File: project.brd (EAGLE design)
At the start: 160 x 100 mm, 42 parts, among them Y1 ABM8-20.000MHZ-B2-T

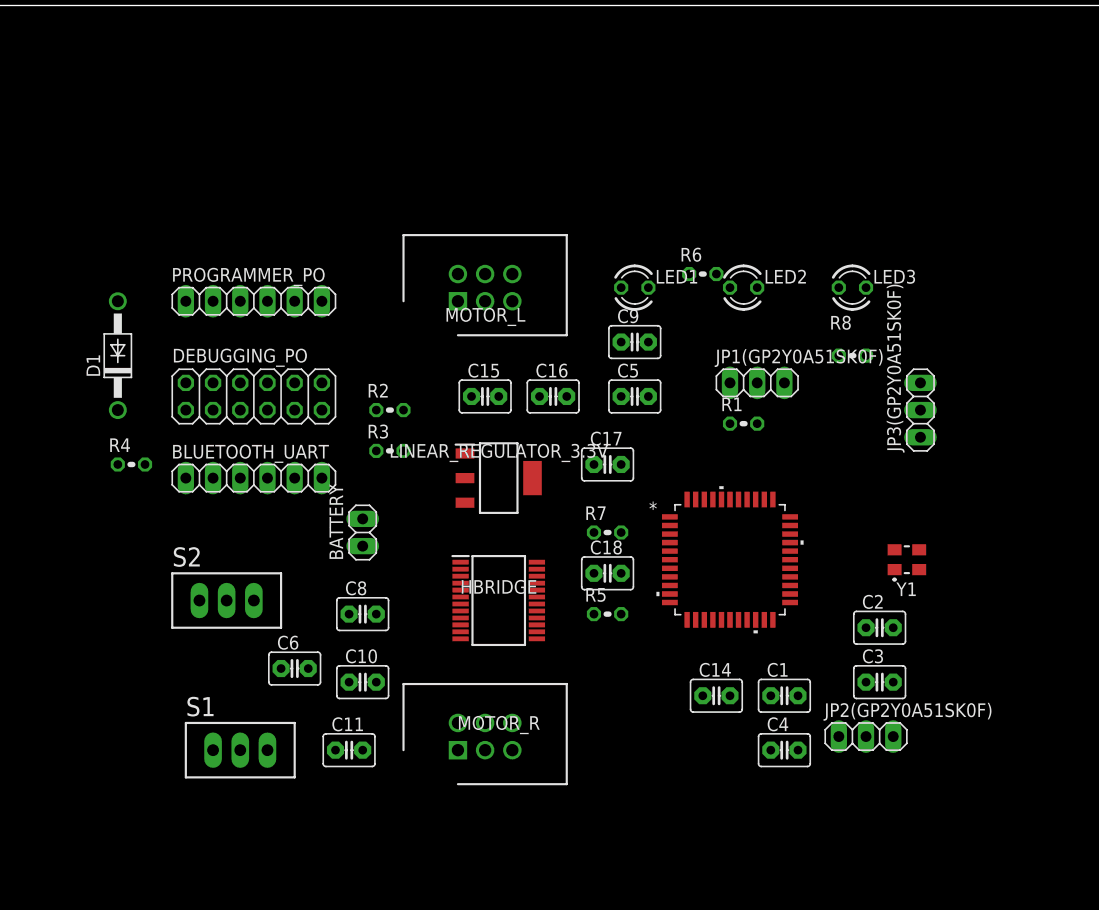
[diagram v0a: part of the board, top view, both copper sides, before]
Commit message: group and place components in board
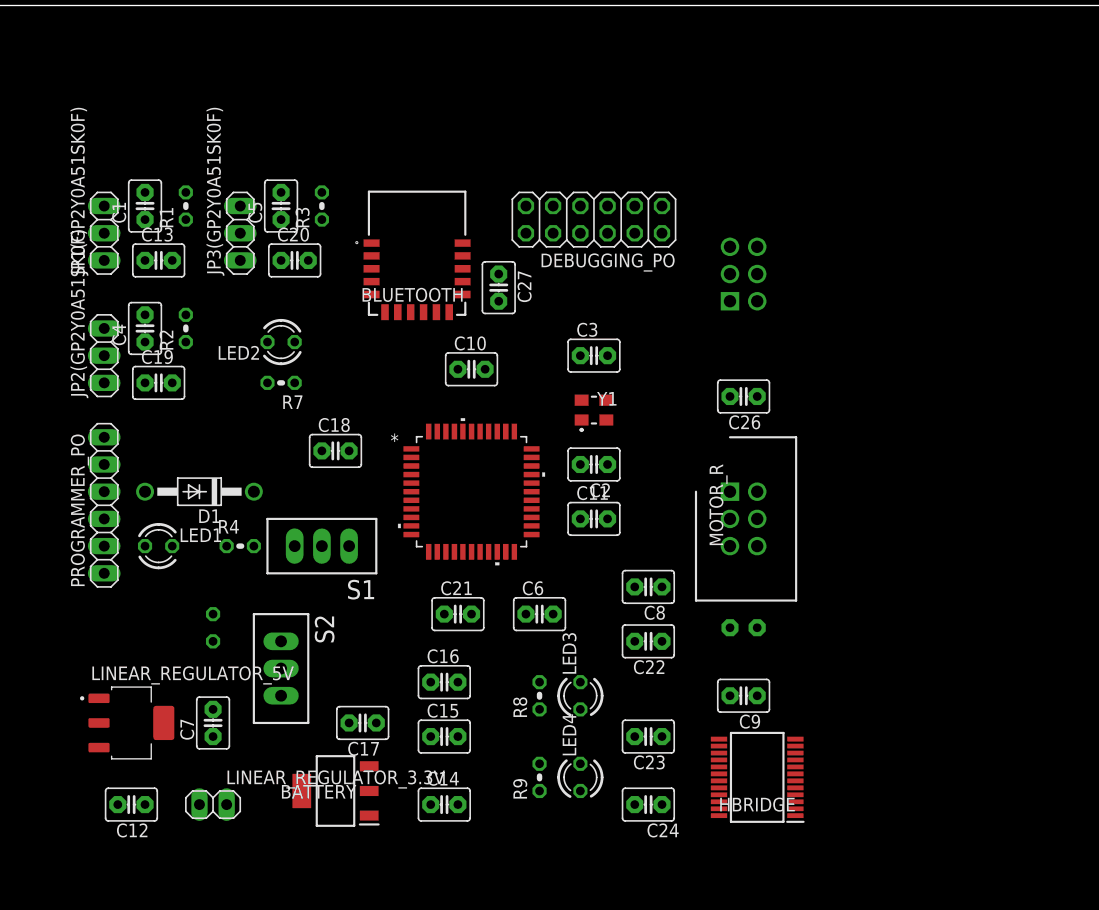
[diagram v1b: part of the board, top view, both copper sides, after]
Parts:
- removed BLUETOOTH_UART: (no value), pinhead:1X06
- removed R6: 10k, rcl:0204V
- added BLUETOOTH: RN4871-I_RM130, RN4871-I_RM130:RN4871
- added C12, C7: 1uF, capacitor-wima:C2.5-3
- added C13, C19, C20, C21, C24, C25, C26, C27: 100nF, capacitor-wima:C2.5-3
- added C22: 0.1uF, capacitor-wima:C2.5-3
- added C23: 10uF, capacitor-wima:C2.5-3
- added LED4: TLLG4400, led:LED3MM
- added LINEAR_REGULATOR_5V: ADP3338AKCZ-5-R7, ADP3338AKCZ-5-R7:SOT230P700X180-4N
- added R9: 10k, rcl:0204V
- C10, C11, C6: value 0.1uF -> 100nF
- C8: value 0.1uF -> 10uF
- moved JP2(GP2Y0A51SK0F) 79.5 mm to (41.9, 67.3), turned to 90 degrees
- moved C1 75.2 mm to (45.7, 81.3), turned to 90 degrees
- moved C4 71.5 mm to (45.7, 69.8), turned to 90 degrees
- moved JP3(GP2Y0A51SK0F) 65.6 mm to (54.6, 78.7)
- moved JP1(GP2Y0A51SK0F) 62.5 mm to (41.9, 78.7), turned to 90 degrees
- moved R1 55.9 mm to (49.5, 81.3), turned to 90 degrees
- moved LED1 50.6 mm to (47.0, 49.5)
- moved LED3 45.8 mm to (86.4, 35.6), turned to 90 degrees
- moved LED2 43.5 mm to (58.4, 68.6), turned to 180 degrees
- moved R8 43.1 mm to (82.5, 35.6), turned to 90 degrees
- moved C3 40.5 mm to (87.6, 67.3)
- moved C5 37.5 mm to (58.4, 81.3), turned to 90 degrees
- moved R5 36.9 mm to (52.1, 41.9), flipped to the bottom, turned to 270 degrees
- moved DEBUGGING_PO 35.8 mm to (87.6, 80.0), turned to 180 degrees
- moved MOTOR_R 35.0 mm to (100.3, 54.6), turned to 270 degrees
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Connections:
- removed net CTS: BLUETOOTH_UART.6, MICROCHIP.10
- removed net ENCA_A: MOTOR_L.5, MOTOR_L.6
- removed net ENCB_A: MOTOR_R.5
- removed net ENCB_B: MOTOR_R.6
- removed net MTRDRV_AI1: HBRIDGE.21
- removed net N$15: MICROCHIP.2, R6.2
- removed net N$16 (its old number): LED1.A, R6.1
- removed net PWMA: DEBUGGING_PO.1, HBRIDGE.23, MICROCHIP.3, R8.2
- removed net PWMB: DEBUGGING_PO.3, HBRIDGE.15, MICROCHIP.14, R7.2
- removed net RTS: BLUETOOTH_UART.3, MICROCHIP.11
- removed net STBY: DEBUGGING_PO.5, HBRIDGE.19, MICROCHIP.1
- removed net VCC: C15.1, C16.1, C17.1, D1.A, HBRIDGE.20, JP1(GP2Y0A51SK0F).1, JP2(GP2Y0A51SK0F).1, JP3(GP2Y0A51SK0F).1, LINEAR_REGULATOR_3.3V.3, PROGRAMMER_PO.2, S2.3
- removed net VDD33: BLUETOOTH_UART.1, C10.1, C11.1, C6.1, MICROCHIP.17, MICROCHIP.18, MICROCHIP.28, MICROCHIP.40, MOTOR_L.4, MOTOR_R.4, PROGRAMMER_PO.1, R4.1, S1.3
- new net 3.3V: BLUETOOTH.14, C10.2, C11.2, C15.1, C16.1, C17.1, C24.1, C25.1, C26.1, C27.1, C6.1, D1.A, HBRIDGE.20, LINEAR_REGULATOR_3.3V.3, MICROCHIP.17, MICROCHIP.28, MICROCHIP.40, MOTOR_L.4, MOTOR_R.4, PROGRAMMER_PO.2, S2.3
- new net 5V: C13.1, C19.1, C20.1, C22.1, C23.1, C7.1, HBRIDGE.19, JP1(GP2Y0A51SK0F).1, JP2(GP2Y0A51SK0F).1, JP3(GP2Y0A51SK0F).1, LINEAR_REGULATOR_5V.2, LINEAR_REGULATOR_5V.4
- new net ENCL_A: MICROCHIP.2, MOTOR_L.5
- new net ENCL_B: MICROCHIP.1, MOTOR_L.6
- new net ENCR_A: MICROCHIP.3, MOTOR_R.5
- new net ENCR_B: MICROCHIP.4, MOTOR_R.6
- new net LED2: MICROCHIP.8, R7.2
- new net N$20: BLUETOOTH.3
- new net N$21: BLUETOOTH.4
- new net N$22: BLUETOOTH.5
- new net N$23: BLUETOOTH.6
- new net N$24: BLUETOOTH.9
- new net N$25: BLUETOOTH.10
- new net N$26: BLUETOOTH.11
- new net N$31: BLUETOOTH.15
- new net N$32: BLUETOOTH.16
- new net N$6: LED4.A, R9.1
- new net N$9: C21.1, LED1.K, PROGRAMMER_PO.1
- new net PGEC1: MICROCHIP.22, PROGRAMMER_PO.5
- new net PGED1: MICROCHIP.21, PROGRAMMER_PO.4
- new net PMW_L: DEBUGGING_PO.1, MICROCHIP.15
- new net PMW_R: MICROCHIP.11
- new net PWM_L: HBRIDGE.23, R8.2
- new net PWM_R: DEBUGGING_PO.3, HBRIDGE.15, R9.2
- net GND: now also BLUETOOTH.13, BLUETOOTH.2, C10.1, C11.1, C12.2, C13.2, C19.2, C20.2, C22.2, C23.2, C24.2, C25.2, C26.2, C27.2, C7.2, DEBUGGING_PO.10, LED4.K, LINEAR_REGULATOR_5V.1; no longer BLUETOOTH_UART.2, C10.2, C11.2, LED1.K
- net MTRDRV_AIN1: now also HBRIDGE.21
- net N$12: now also LED1.A, R4.1, S1.3; no longer MICROCHIP.22, PROGRAMMER_PO.4
- net N$13: now also C21.2, MICROCHIP.18; no longer MICROCHIP.21, PROGRAMMER_PO.5
- net N$27: now also BLUETOOTH.12; no longer DEBUGGING_PO.10
- net RX: now also BLUETOOTH.7, MICROCHIP.38; no longer BLUETOOTH_UART.4, MICROCHIP.9
- net TX: now also BLUETOOTH.8, MICROCHIP.37; no longer BLUETOOTH_UART.5, MICROCHIP.8
- net VM: now also C12.1, LINEAR_REGULATOR_5V.3

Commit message: route board
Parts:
- moved C25 21.6 mm to (101.6, 63.5)
- moved C26 21.6 mm to (101.6, 41.9), flipped to the bottom
- moved MOTOR_L 21.6 mm to (100.3, 50.8)
- moved C6 17.6 mm to (67.3, 34.3), turned to 90 degrees
- moved MOTOR_R 16.5 mm to (100.3, 71.1), flipped to the bottom, turned to 90 degrees
- moved LED3 10.9 mm to (80.0, 26.7)
- moved R8 8.98 mm to (83.8, 26.7)
- moved LED2 8.13 mm to (53.3, 62.2)
- moved LED4 8.13 mm to (80.0, 33.0)
- moved C20 5.68 mm to (54.6, 73.7)
- moved C19 5.39 mm to (43.2, 61.0)
- moved R9 5.24 mm to (83.8, 33.0)
- moved C17 5.24 mm to (71.1, 34.3), turned to 90 degrees
- moved C13 4.58 mm to (43.2, 73.7)
- moved C18 4.58 mm to (61.0, 62.2)
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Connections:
- removed net B01: HBRIDGE.12
- removed net PMW_L: DEBUGGING_PO.1, MICROCHIP.15
- removed net PMW_R: MICROCHIP.11
- net AN0: now also MICROCHIP.20; no longer MICROCHIP.19
- net AN1: now also MICROCHIP.19; no longer MICROCHIP.20
- net BO1: now also HBRIDGE.11, HBRIDGE.12
- net ENCL_A: now also MICROCHIP.1; no longer MICROCHIP.2
- net ENCL_B: now also MICROCHIP.2; no longer MICROCHIP.1
- net N$16: now also MICROCHIP.12; no longer MICROCHIP.43
- net PGEC1: now also MICROCHIP.9; no longer MICROCHIP.22
- net PGED1: now also MICROCHIP.10; no longer MICROCHIP.21
- net PWM_L: now also MICROCHIP.15
- net PWM_R: now also MICROCHIP.11; no longer DEBUGGING_PO.3
- net RX: now also MICROCHIP.44; no longer MICROCHIP.38
- net TX: now also MICROCHIP.43; no longer MICROCHIP.37
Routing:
- net 3.3V: track 0.00 -> 246.0 mm, vias 0 -> 1
- net 5V: track 0.00 -> 137.6 mm, vias 0 -> 3
- net VM: track 0.00 -> 97.3 mm
- net AN0: track 0.00 -> 95.3 mm, vias 0 -> 2
- net AN1: track 0.00 -> 90.9 mm, vias 0 -> 6
- net MTRDRV_AIN2: track 0.00 -> 79.7 mm, vias 0 -> 2
- net MTRDRV_AIN1: track 0.00 -> 78.9 mm, vias 0 -> 2
- net MTRDRV_BIN1: track 0.00 -> 76.3 mm, vias 0 -> 4
- net MTRDRV_BIN2: track 0.00 -> 76.2 mm, vias 0 -> 4
- net AN4: track 0.00 -> 69.9 mm, vias 0 -> 2
- net ENCL_B: track 0.00 -> 57.4 mm
- net ENCR_B: track 0.00 -> 56.2 mm
- net ENCL_A: track 0.00 -> 51.1 mm
- net PWM_R: track 0.00 -> 50.6 mm, vias 0 -> 4
- net ENCR_A: track 0.00 -> 49.0 mm
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- added copper zone on layer 1, net GND
- added copper zone on layer 16, net GND
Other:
- board size 160 x 100 mm -> 71.1 x 63.5 mm

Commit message: Progress!
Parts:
- removed BATTERY: (no value), pinhead:1X02
- removed C12, C7: 1uF, capacitor-wima:C2.5-3
- removed LINEAR_REGULATOR_5V: ADP3338AKCZ-5-R7, ADP3338AKCZ-5-R7:SOT230P700X180-4N
- added C29, C30, C31: C0805J104K1RACAUTO, C0805J104K1RACAUTO:CAPC2012X140N
- added IC1: ADP3338AKCZ-5-R7, ADP3338AKCZ-5-R7:SOT230P700X180-4N
- added J1: 22-23-2021, 22-23-2021:SHDR2W87P0X254_1X2_493X635X110
- added R10, R6: 4.7k, rcl:0204V
- LED1, LED2, LED3, LED4: value TLLG4400 -> APT3216LSECK_J3-PRV; device led:LED3MM -> APT3216LSECK_J3-PRV:LEDC3216X95N
- R1: value 10k -> 4.7k
- S1, S2: value TL32PO -> B3F-1020; device switch:TL3XPO -> B3F-1020:B3F1000
- moved MOTOR_R 91.7 mm to (21.6, 24.1), flipped to the top, turned to 0 degrees
- moved MOTOR_L 86.4 mm to (17.8, 76.2), flipped to the top, turned to 0 degrees
- moved C1 82.1 mm to (15.2, 5.08), turned to 0 degrees
- moved C5 79.1 mm to (33.0, 6.35), turned to 0 degrees
- moved R3 76.1 mm to (20.3, 17.8), turned to 0 degrees
- moved R1 74.1 mm to (11.4, 17.8), turned to 0 degrees
- moved D1 72.7 mm to (123.2, 30.5), turned to 0 degrees
- moved C26 69.5 mm to (41.9, 6.35), flipped to the top, turned to 0 degrees
- moved C4 66.3 mm to (22.9, 5.08), turned to 0 degrees
- moved LED1 65.6 mm to (113.0, 35.6), turned to 0 degrees
- moved PROGRAMMER_PO 63.3 mm to (92.7, 88.9), turned to 0 degrees
- moved R4 63.1 mm to (114.3, 30.5), turned to 0 degrees
- moved R2 59.5 mm to (16.5, 17.8), turned to 0 degrees
- moved C25 57.4 mm to (47.0, 45.7), flipped to the top
- moved C15 55.4 mm to (55.9, 86.4), turned to 0 degrees
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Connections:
- net N$24 renamed RTS
- net N$26 renamed CTS
- net 3.3V: now also R10.2, R6.2
- net 5V: now also C29.1, IC1.4; no longer C7.1, LINEAR_REGULATOR_5V.2, LINEAR_REGULATOR_5V.4
- net GND: now also C29.2, C30.2, C31.2, IC1.1, J1.2, LED2.1, LED3.1, LED4.1, S1.4; no longer BATTERY.2, C12.2, C7.2, LED2.K, LED3.K, LED4.K, LINEAR_REGULATOR_5V.1, S1.2
- net N$10: now also LED3.2; no longer LED3.A
- net N$11: now also LED2.2; no longer LED2.A
- net N$12: now also LED1.2, S1.1; no longer LED1.A, S1.3
- net N$25: now also C31.1, R10.1
- net N$27: now also R6.1
- net N$6: now also LED4.2; no longer LED4.A
- net N$9: now also LED1.1; no longer LED1.K
- net PGEC1: now also MICROCHIP.22
- net PGED1: now also MICROCHIP.21
- net VM: now also C30.1, IC1.3, J1.1; no longer BATTERY.1, C12.1, LINEAR_REGULATOR_5V.3
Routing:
- net 3.3V: track 246.0 -> 0.00 mm, vias 1 -> 0
- net 5V: track 137.6 -> 32.8 mm, vias 3 -> 0
- net AN0: track 95.3 -> 0.00 mm, vias 2 -> 0
- net AN1: track 90.9 -> 0.00 mm, vias 6 -> 0
- net MTRDRV_AIN2: track 79.7 -> 0.00 mm, vias 2 -> 0
- net MTRDRV_AIN1: track 78.9 -> 0.00 mm, vias 2 -> 0
- net MTRDRV_BIN1: track 76.3 -> 0.00 mm, vias 4 -> 0
- net MTRDRV_BIN2: track 76.2 -> 0.00 mm, vias 4 -> 0
- net AN4: track 69.9 -> 0.00 mm, vias 2 -> 0
- net VM: track 97.3 -> 37.3 mm
- net ENCL_B: track 57.4 -> 0.00 mm
- net ENCR_B: track 56.2 -> 0.00 mm
- net ENCL_A: track 51.1 -> 0.00 mm
- net PWM_R: track 50.6 -> 0.00 mm, vias 4 -> 0
- net ENCR_A: track 49.0 -> 0.00 mm
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- removed copper zone on layer 1, net GND
- removed copper zone on layer 16, net GND
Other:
- board size 71.1 x 63.5 mm -> 160 x 100 mm

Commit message: Progress!
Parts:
- removed C10, C11, C13, C16, C17, C19, C20, C21, C24, C25, C26, C27, C4, C5, C6: 100nF, capacitor-wima:C2.5-3
- removed C15: 0.1µF, capacitor-wima:C2.5-3
- removed C22: 0.1uF, capacitor-wima:C2.5-3
- added C12, C7: 0805YC106KAT2A, 0805YC106KAT2A:CAPC2012X94N
- added C28, C32, C33, C34, C35, C36, C37, C38, C39, C40, C41, C42, C43, C44, C46: C0805J104K1RACAUTO, C0805J104K1RACAUTO:CAPC2012X140N
- C1: value 100nF -> C0805J104K1RACAUTO; device capacitor-wima:C2.5-3 -> C0805J104K1RACAUTO:CAPC2012X140N
- C14: value 0.33µF -> C0805J104K1RACAUTO; device capacitor-wima:C2.5-3 -> C0805J104K1RACAUTO:CAPC2012X140N
- C23: value 10uF -> C0805J104K1RACAUTO; device capacitor-wima:C2.5-3 -> C0805J104K1RACAUTO:CAPC2012X140N
- C30: value C0805J104K1RACAUTO -> 1µF
- C8: value 10uF -> 0805YC106KAT2A; device capacitor-wima:C2.5-3 -> 0805YC106KAT2A:CAPC2012X94N
- C9: value 10uF -> 08053C334KAZ2A; device capacitor-wima:C2.5-3 -> 08053C334KAZ2A:CAPC2012X152N
- moved C1 148.3 mm to (-119.4, -57.1)
- moved C14 106.5 mm to (-5.08, -11.4), turned to 0 degrees
- moved C8 96.8 mm to (-5.08, -8.89), turned to 0 degrees
- moved C23 43.4 mm to (76.2, 52.1), turned to 90 degrees
- moved C30 24.0 mm to (76.2, 61.0), turned to 90 degrees
- moved C9 10.2 mm to (76.2, 55.9)
- moved JP1(GP2Y0A51SK0F) 3.81 mm to (82.5, 74.9)
- moved JP2(GP2Y0A51SK0F) 3.81 mm to (95.2, 67.3)
- moved LINEAR_REGULATOR_3.3V 3.81 mm to (82.5, 54.6)
- moved IC1 1.27 mm to (82.5, 62.2)
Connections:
- net 3.3V: now also C1.1, C14.1, C23.1, C28.1, C38.1, C39.1, C40.1, C42.1, C43.1, C44.1; no longer C10.2, C11.2, C15.1, C16.1, C17.1, C24.1, C25.1, C26.1, C27.1, C6.1
- net 5V: now also C35.1, C36.1, C37.1, C46.1, C8.1; no longer C13.1, C19.1, C20.1, C22.1, C23.1
- net AN0: now also C32.1; no longer C1.1
- net AN1: now also C33.1; no longer C4.1
- net AN4: now also C34.1; no longer C5.1
- net GND: now also C12.2, C28.2, C32.2, C33.2, C34.2, C35.2, C36.2, C37.2, C38.2, C39.2, C40.2, C42.2, C43.2, C44.2, C46.2, C7.2; no longer C10.1, C11.1, C13.2, C15.2, C16.2, C17.2, C19.2, C20.2, C22.2, C24.2, C25.2, C26.2, C27.2, C4.2, C5.2, C6.2
- net N$13: now also C41.2; no longer C21.2
- net N$9: now also C41.1; no longer C21.1
- net VM: now also C12.1, C7.1; no longer C14.1, C8.1
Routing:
- net 5V: track 32.8 -> 0.00 mm
- net VM: track 37.3 -> 44.8 mm
- net 3.3V: track 0.00 -> 3.63 mm

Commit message: Progress
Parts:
- removed R10, R5, R6: 4.7k, rcl:0204V
- removed R4: 47k, rcl:0204V
- added R11, R12, R13, R14: ERA-6ARW472V, ERA-6ARW472V:ERA6AEB101V
- D1: value 1N4004 -> 1N4148WS-HG3-08; device diode:DO41-10 -> 1N4148WS-HG3-08:SOD2713X115N
- R1: value 4.7k -> ERA-6ARW473V; device rcl:0204V -> ERA-6ARW473V:ERA6AEB101V
- moved C41 230.9 mm to (138.4, 29.2), flipped to the bottom
- moved C39 223.1 mm to (137.2, 49.5)
- moved C38 211.2 mm to (138.4, 31.8), flipped to the bottom
- moved C42 184.9 mm to (66.0, 58.4), turned to 90 degrees
- moved C37 168.6 mm to (88.9, 54.6), turned to 270 degrees
- moved C36 164.9 mm to (90.2, 58.4), turned to 270 degrees
- moved C35 161.7 mm to (90.2, 64.8), turned to 90 degrees
- moved C28 126.1 mm to (88.9, 50.8), turned to 90 degrees
- moved C14 114.8 mm to (91.4, 50.8), turned to 90 degrees
- moved R1 75.2 mm to (81.3, 45.7), turned to 90 degrees
- moved C18 73.0 mm to (120.7, 39.4), turned to 90 degrees
- moved C29 66.0 mm to (87.6, 63.5), turned to 90 degrees
- moved MICROCHIP 65.2 mm to (137.2, 40.6)
- moved R8 50.1 mm to (12.7, 34.3)
- moved C2 49.0 mm to (96.5, 16.5)
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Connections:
- new net STBY: HBRIDGE.19
- net 3.3V: now also D1.2, R13.2, R14.1; no longer D1.A, R10.2, R6.2
- net 5V: no longer HBRIDGE.19
- net AN0: now also R11.1; no longer R1.2
- net GND: now also R11.2, R12.2; no longer R1.1, R5.1
- net N$12: now also R1.2; no longer R4.1
- net N$16: now also R12.1; no longer R5.2
- net N$25: now also R14.2; no longer R10.1
- net N$27: now also R13.1; no longer R6.1
- net N$5: now also D1.1, R1.1; no longer D1.C, R4.2
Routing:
- net 3.3V: track 3.63 -> 69.3 mm
- net 5V: track 0.00 -> 27.0 mm
- net N$12: track 0.00 -> 9.90 mm
- net N$5: track 0.00 -> 4.46 mm
- net VM: track 44.8 -> 48.9 mm, vias 0 -> 1

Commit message: Progress
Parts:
- removed C18: 4.7uF, capacitor-wima:C2.5-3
- removed R2, R3, R7, R8, R9: 10k, rcl:0204V
- added C4: MBAST21GBC7475KTCA01, MBAST21GBC7475KTCA01:CAPC2114X145N
- added R10, R15, R4, R5, R6: RNCE0805BTE10K0, RNCE0805BTE10K0:RESC2012X65N
- moved C40 147.8 mm to (59.7, 21.6)
- moved MICROCHIP 100.5 mm to (36.8, 34.3), turned to 90 degrees
- moved C38 91.8 mm to (49.5, 8.89), flipped to the top, turned to 270 degrees
- moved C39 91.2 mm to (48.3, 29.2), turned to 180 degrees
- moved C41 88.7 mm to (52.1, 8.89), flipped to the top, turned to 90 degrees
- moved LED4 46.2 mm to (59.7, 50.8), turned to 270 degrees
- moved LED2 43.0 mm to (52.1, 50.8), turned to 270 degrees
- moved LED3 37.4 mm to (55.9, 50.8), turned to 270 degrees
- moved C3 21.6 mm to (105.4, 5.08)
- moved C2 18.8 mm to (105.4, 0.00), turned to 180 degrees
- moved BLUETOOTH 17.0 mm to (21.6, 57.1)
- moved Y1 16.9 mm to (113.0, 2.54)
- moved C14 1.27 mm to (92.7, 50.8)
- moved C28 1.27 mm to (90.2, 50.8)
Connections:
- new net LED3: MICROCHIP.37, R10.1
- new net LED4: MICROCHIP.36, R15.1
- net AN1: now also R4.1; no longer R2.2
- net AN4: now also R5.1; no longer R3.2
- net GND: now also C4.1, R4.2, R5.2; no longer C18.2, R2.1, R3.1
- net LED2: now also MICROCHIP.38, R6.1; no longer MICROCHIP.8, R7.2
- net N$10: now also R10.2; no longer R8.1
- net N$11: now also R6.2; no longer R7.1
- net N$6: now also R15.2; no longer R9.1
- net N$7: now also C4.2; no longer C18.1
- net PWM_L: no longer R8.2
- net PWM_R: no longer R9.2
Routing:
- net 3.3V: track 69.3 -> 55.0 mm

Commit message: Saving Progress
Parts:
- removed DEBUGGING_PO: (no value), pinhead:2X06
- C2, C3: value 22pF -> 08055A300JAT2A; device capacitor-wima:C2.5-3 -> 08055A300JAT2A:CAPC2012X94N
- moved C46 233.7 mm to (86.4, 67.3), turned to 90 degrees
- moved C44 186.9 mm to (49.5, 62.2), turned to 180 degrees
- moved C1 185.7 mm to (31.8, 50.8), turned to 180 degrees
- moved C43 165.1 mm to (38.1, 52.1), turned to 270 degrees
- moved C8 121.0 mm to (88.9, 67.3), turned to 90 degrees
- moved C2 62.5 mm to (67.3, 49.5), turned to 0 degrees
- moved Y1 60.2 mm to (72.4, 47.0)
- moved C3 56.6 mm to (67.3, 47.0), turned to 180 degrees
- moved PROGRAMMER_PO 55.5 mm to (77.5, 35.6), turned to 180 degrees
- moved C41 37.4 mm to (63.5, 44.5), turned to 180 degrees
- moved C38 36.9 mm to (66.0, 41.9)
- moved C40 30.7 mm to (55.9, 52.1)
- moved MOTOR_L 25.9 mm to (57.1, 69.8), turned to 180 degrees
- moved C4 24.7 mm to (50.8, 29.2), turned to 90 degrees
- moved LED2 21.6 mm to (53.3, 29.2), turned to 90 degrees
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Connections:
- removed net N$28: DEBUGGING_PO.12
- net AN0: no longer DEBUGGING_PO.7
- net AN1: no longer DEBUGGING_PO.9
- net AN4: no longer DEBUGGING_PO.11
- net GND: no longer DEBUGGING_PO.10
- net LED2: now also MICROCHIP.8; no longer MICROCHIP.38
- net LED3: now also MICROCHIP.9; no longer MICROCHIP.37
- net LED4: now also MICROCHIP.10; no longer MICROCHIP.36
- net MTRDRV_AIN1: now also MICROCHIP.26; no longer DEBUGGING_PO.2, MICROCHIP.27
- net MTRDRV_AIN2: now also MICROCHIP.27; no longer DEBUGGING_PO.4, MICROCHIP.26
- net MTRDRV_BIN1: no longer DEBUGGING_PO.6
- net MTRDRV_BIN2: no longer DEBUGGING_PO.8
- net N$1: now also C2.1; no longer C3.1
- net N$2: now also C3.2; no longer C2.2
- net N$3: now also C3.1; no longer C2.1
- net N$4: now also C2.2; no longer C3.2
- net PGEC1: no longer MICROCHIP.9
- net PGED1: no longer MICROCHIP.10
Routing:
- net 3.3V: track 55.0 -> 157.7 mm, vias 0 -> 4
- net N$1: track 0.00 -> 17.5 mm, vias 0 -> 2
- net N$2: track 0.00 -> 16.1 mm, vias 0 -> 2
- net BO1: track 0.00 -> 15.9 mm, vias 0 -> 2
- net MTRDRV_AIN2: track 0.00 -> 14.5 mm
- net BO2: track 0.00 -> 13.7 mm, vias 0 -> 2
- net MTRDRV_AIN1: track 0.00 -> 13.5 mm
- net 5V: track 27.0 -> 40.5 mm
- net MTRDRV_BIN1: track 0.00 -> 11.4 mm
- net N$7: track 0.00 -> 11.0 mm
- net AO2: track 0.00 -> 10.6 mm
- net MTRDRV_BIN2: track 0.00 -> 10.0 mm
- net AO1: track 0.00 -> 9.98 mm
- net N$9: track 0.00 -> 7.92 mm
- net N$4: track 0.00 -> 6.09 mm
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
